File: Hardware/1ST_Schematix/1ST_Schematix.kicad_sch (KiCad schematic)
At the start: 6 parts, among them SW101 SW_Push

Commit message: Update before INT
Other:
- sheet STM32 ports: added TOF1_GPIO, TOF1_XST, TOF2_GPIO, TOF2_XST; removed none
- sheet Sensor ports: added none; removed VM

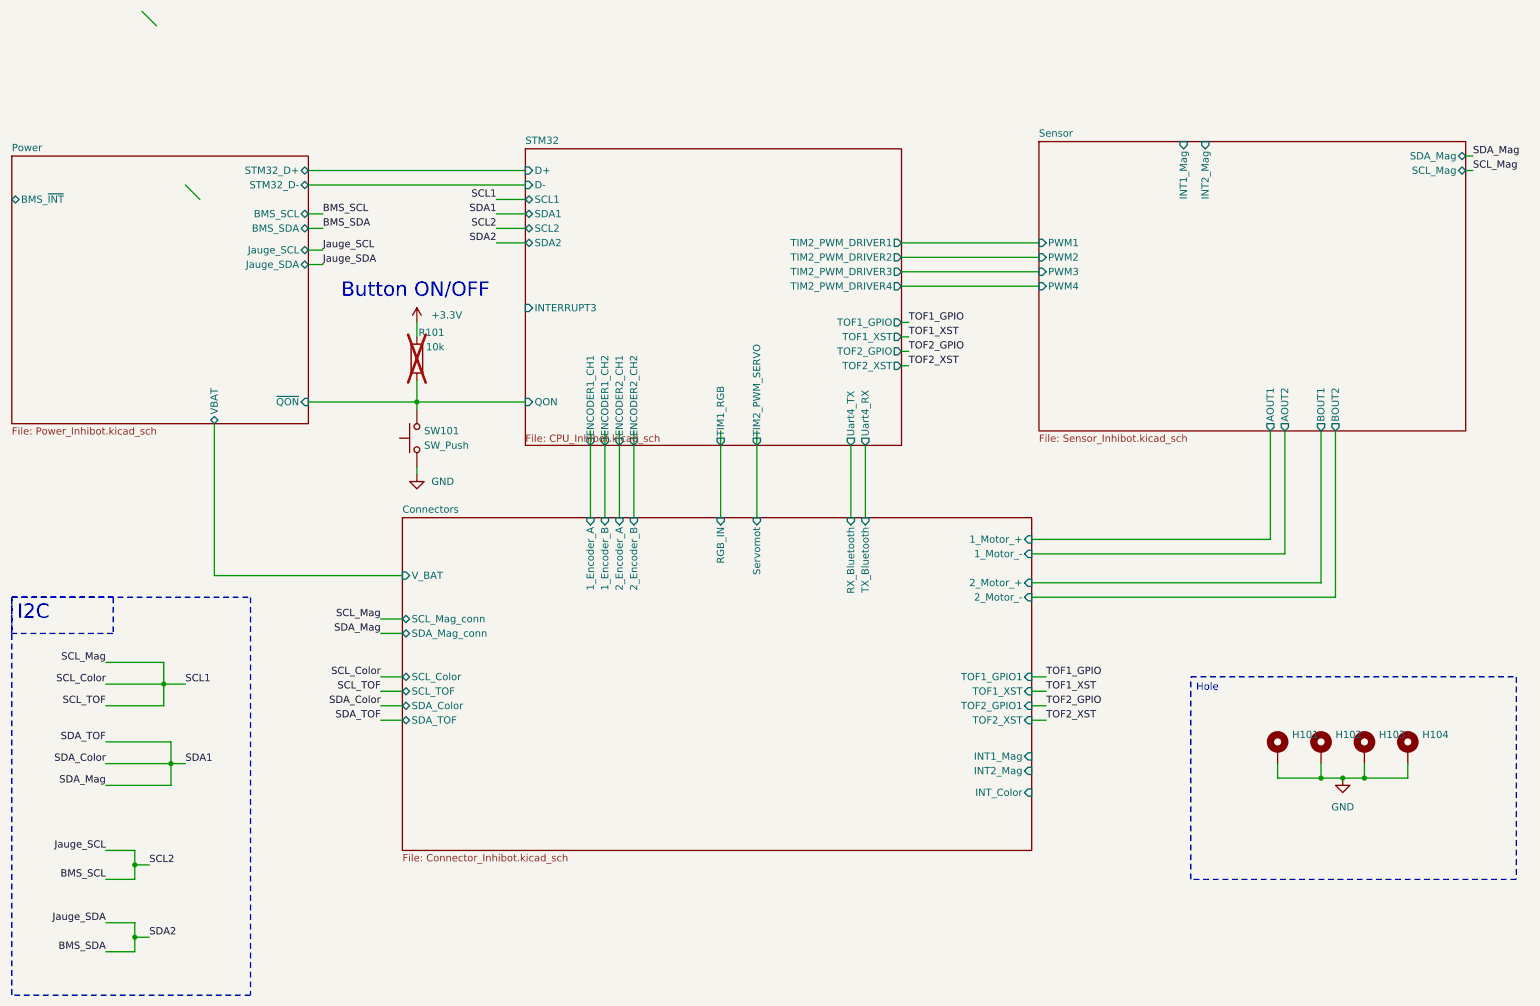
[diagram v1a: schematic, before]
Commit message: Update KiCad and STM32CubeMX
Ready for the check-in
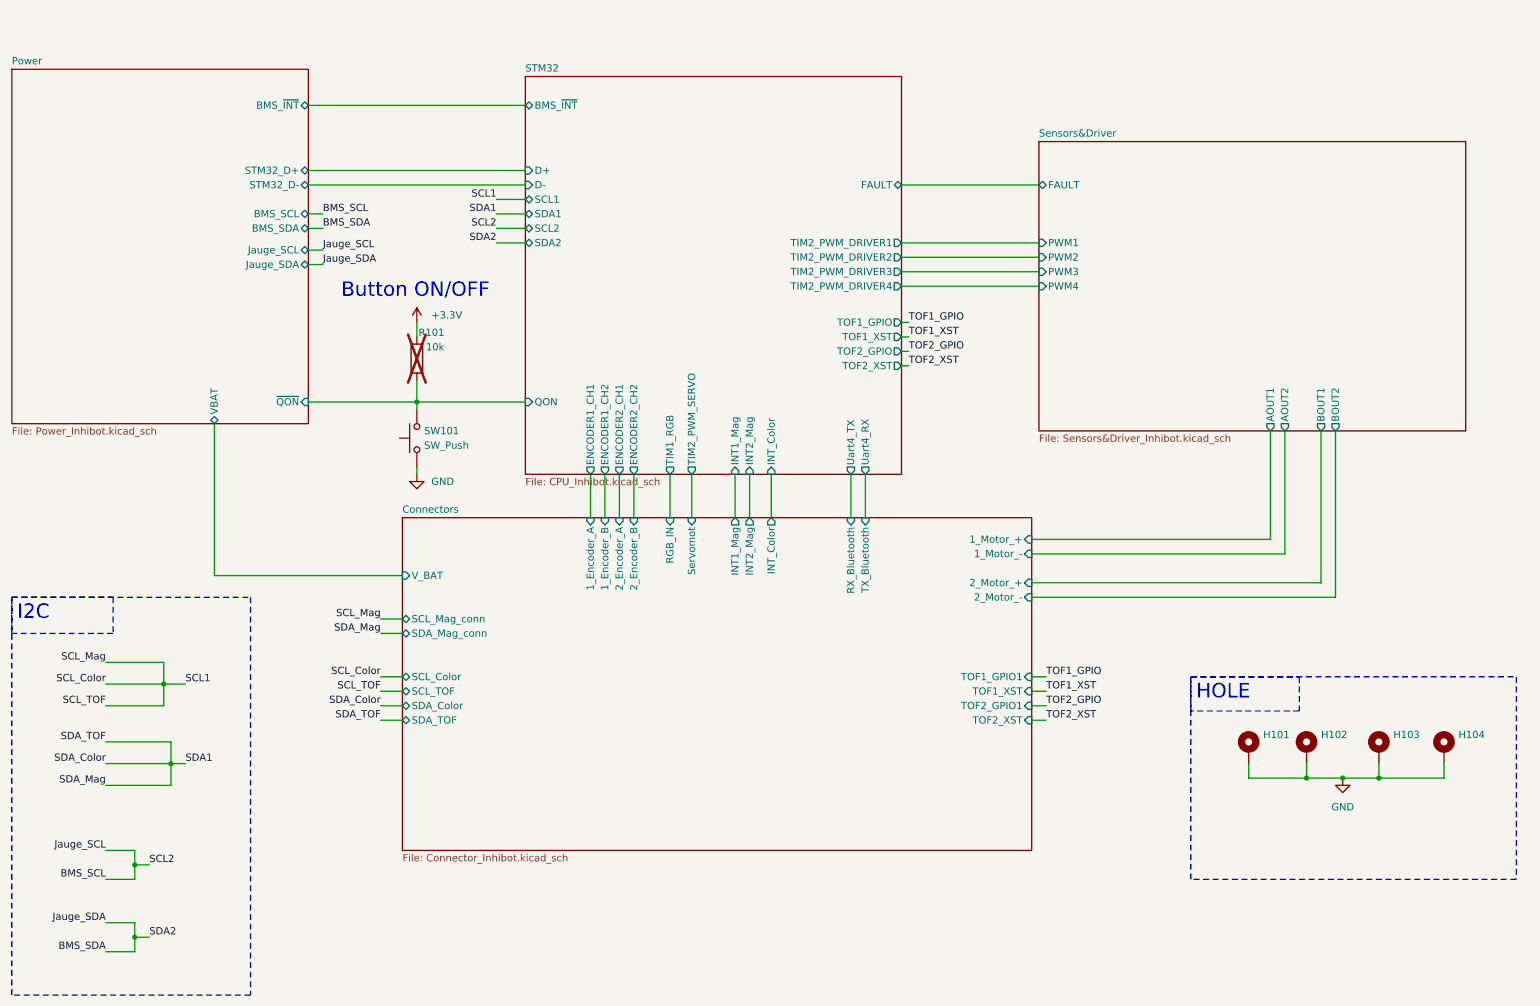
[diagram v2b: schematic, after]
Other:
- sheet Sensor renamed Sensors&Driver
- sheet STM32 ports: added BMS_~{INT}, FAULT, INT1_Mag, INT2_Mag, INT_Color; removed INTERRUPT3
- sheet Sensors&Driver: file Sensor_Inhibot.kicad_sch -> Sensors&Driver_Inhibot.kicad_sch
- sheet Sensors&Driver ports: added FAULT; removed INT1_Mag, INT2_Mag, SCL_Mag, SDA_Mag
- moved on the sheet: H101, H102, H103, H104

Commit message: schematic review with esteemed professor
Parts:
- R101: footprint Resistor_SMD:R_0402_1005Metric_Pad0.72x0.64mm_HandSolder -> Resistor_SMD:R_0603_1608Metric_Pad0.98x0.95mm_HandSolder
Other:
- sheet STM32 ports: added ESP32_RX, ESP32_TX; removed Uart4_RX, Uart4_TX
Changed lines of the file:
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@@
 			)
 		)
-		(property "Footprint" "Resistor_SMD:R_0402_1005Metric_Pad0.72x0.64mm_HandSolder"
+		(property "Footprint" "Resistor_SMD:R_0603_1608Metric_Pad0.98x0.95mm_HandSolder"
 			(at 86.868 69.85 90)
 			(hide yes)
@@
 			)
 		)
-		(pin "Uart4_RX" output
-			(at 163.83 90.17 270)
-			(effects
-				(font
-					(size 1.27 1.27)
-				)
-				(justify left)
-			)
-		)
-		(pin "Uart4_TX" output
-			(at 161.29 90.17 270)
-			(effects
-				(font
-					(size 1.27 1.27)
-				)
-				(justify left)
-			)
-		)
 		(pin "TIM1_RGB" output
 			(at 129.54 90.17 270)
@@
 			(effects
 				(font
+					(size 1.27 1.27)
+				)
+				(justify left)
+			)
+		)
+		(pin "ESP32_RX" output
+			(at 163.83 90.17 270)
+			(effects
+				(font
+					(size 1.27 1.27)
+				)
+				(justify left)
+			)
+		)
+		(pin "ESP32_TX" output
+			(at 161.29 90.17 270)
+			(effects
+				(font

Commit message: routage à faire vérifier
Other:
- sheet Connectors ports: added Servomot1, Servomot2; removed Servomot
- sheet STM32 ports: added TIM2_PWM_SERVO1, TIM2_PWM_SERVO2; removed TIM2_PWM_SERVO
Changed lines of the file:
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@@
+	(wire
+		(pts
+			(xy 135.89 90.17) (xy 135.89 97.79)
+		)
+		(stroke
+			(width 0)
+			(type default)
+		)
+	)
 	(wire
 		(pts
@@
 			)
 		)
-		(pin "Servomot" input
-			(at 133.35 97.79 90)
-			(effects
-				(font
-					(size 1.27 1.27)
-				)
-				(justify right)
-			)
-		)
 		(pin "V_BAT" input
 			(at 82.55 107.95 180)
@@
 		(pin "TX_Bluetooth" input
 			(at 163.83 97.79 90)
+			(effects
+				(font
+					(size 1.27 1.27)
+				)
+				(justify right)
+			)
+		)
+		(pin "Servomot1" input
+			(at 135.89 97.79 90)
+			(effects
+				(font
+					(size 1.27 1.27)
+				)
+				(justify right)
+			)
+		)
+		(pin "Servomot2" input
+			(at 133.35 97.79 90)
 			(effects
 				(font
@@
 			)
 		)
-		(pin "TIM2_PWM_SERVO" output
-			(at 133.35 90.17 270)
-			(effects
-				(font
-					(size 1.27 1.27)
-				)
-				(justify left)
-			)
-		)
 		(pin "TIM1_RGB" output
 			(at 129.54 90.17 270)
@@
 			(effects
 				(font
+					(size 1.27 1.27)
+				)
+				(justify left)
+			)
+		)
+		(pin "TIM2_PWM_SERVO1" output
+			(at 135.89 90.17 270)
+			(effects
+				(font
+					(size 1.27 1.27)
+				)
+				(justify left)
+			)
+		)
+		(pin "TIM2_PWM_SERVO2" output
+			(at 133.35 90.17 270)
+			(effects
+				(font
